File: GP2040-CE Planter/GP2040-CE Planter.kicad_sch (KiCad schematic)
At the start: 57 parts, among them J1 USB_B, J2 USB_A, J3 USB_A, J4 USB_A, J5 USB_A, J6 USB_A, J7 Conn_01x02, U1 TUSB4041IPAPR, U3 TPS2561ADRCR, U4 TPS2561ADRCR, U5 PTMUXHS221NKGR

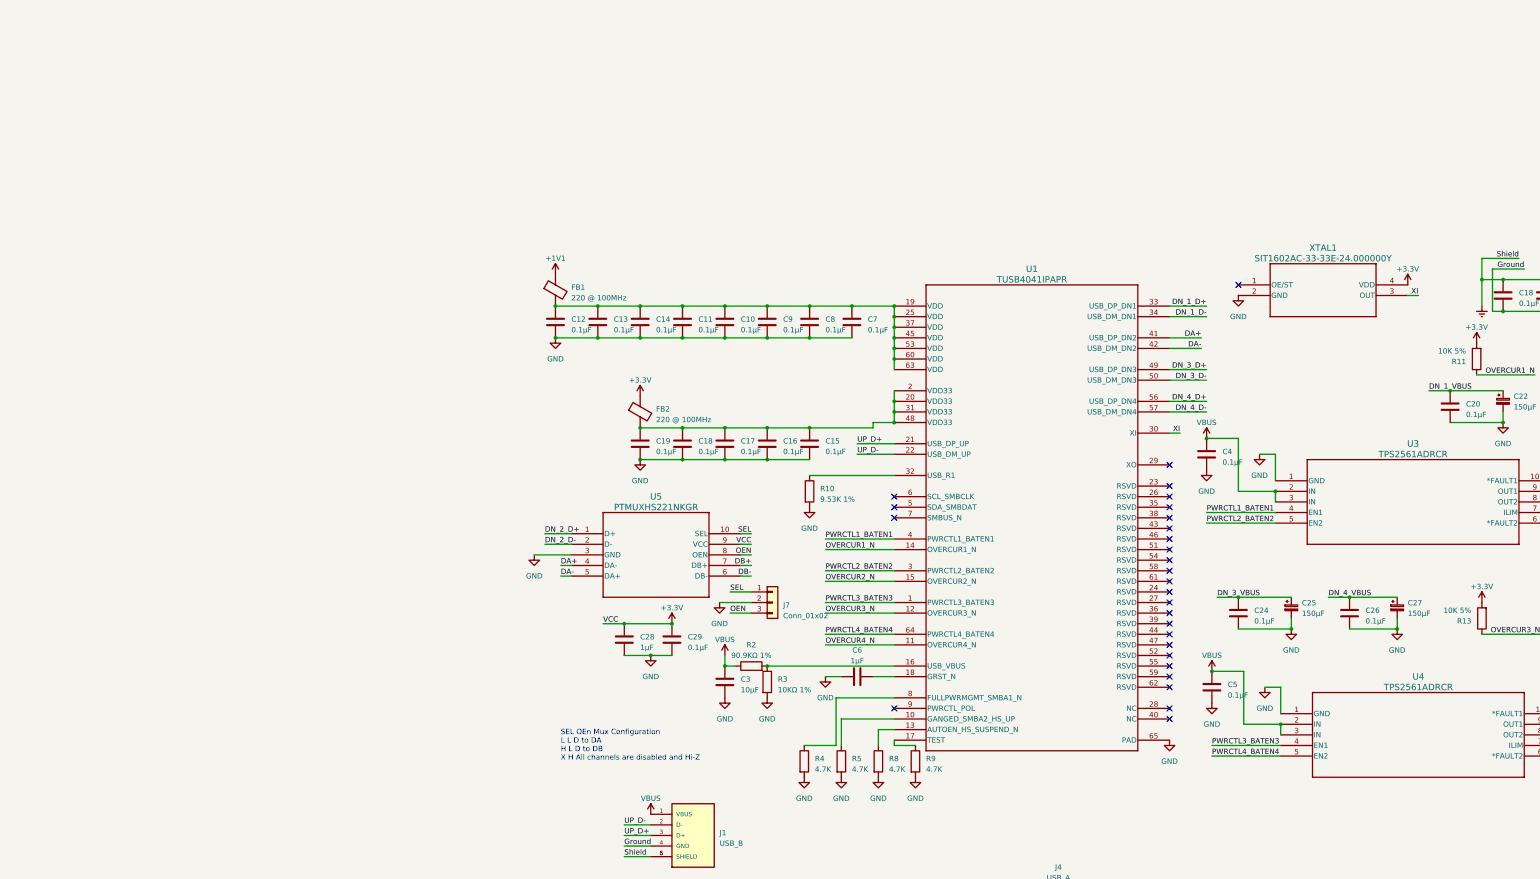
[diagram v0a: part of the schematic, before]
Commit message: Replacing out of stock with instock components
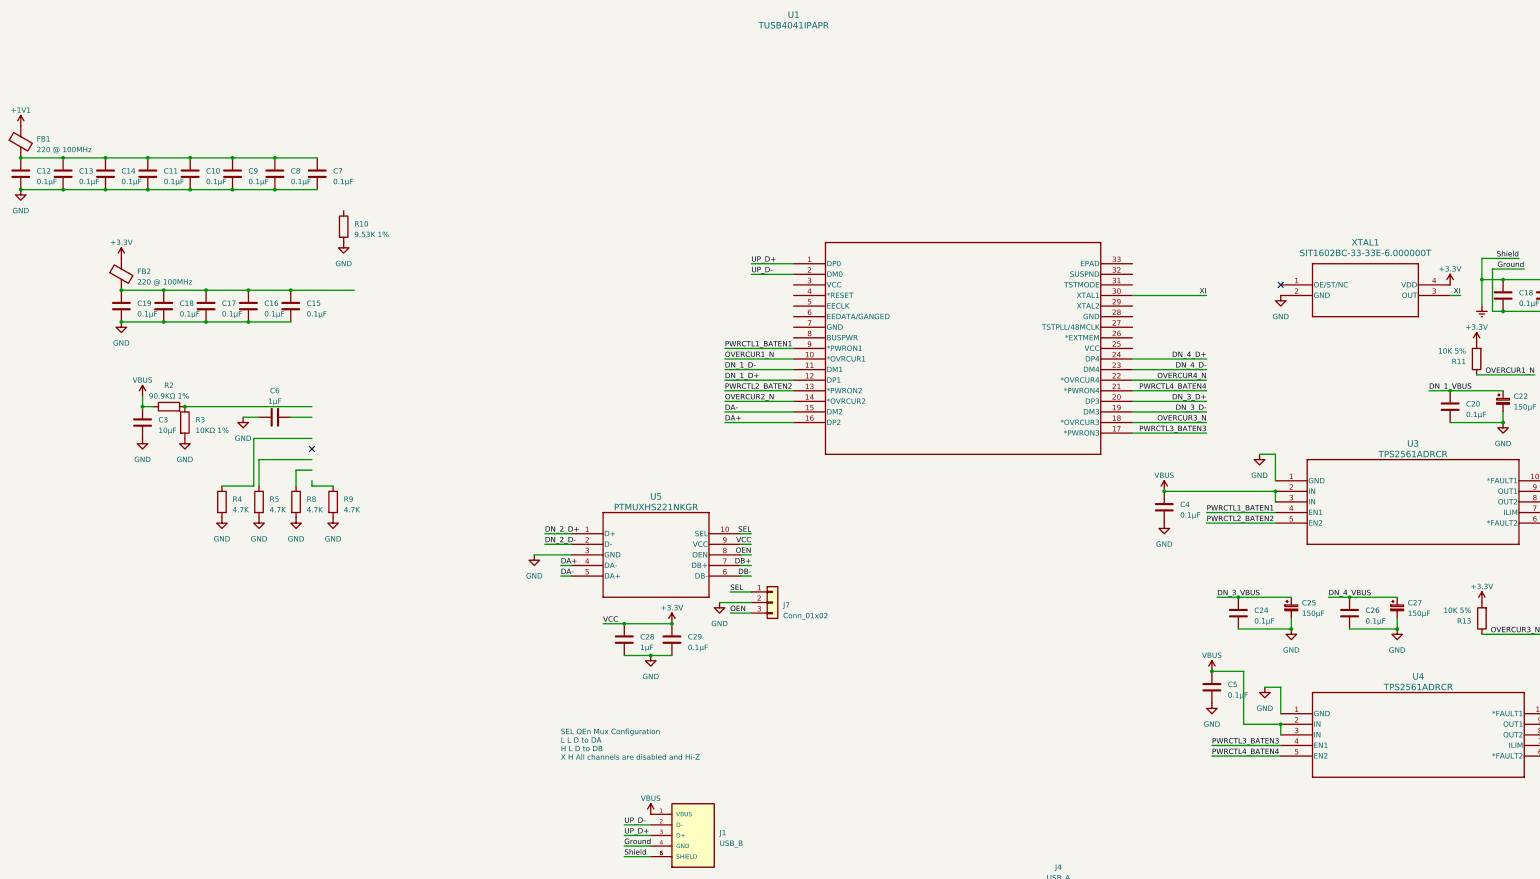
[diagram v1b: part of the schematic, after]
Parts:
- U1: footprint GP2040-CE-Tester:TUSB4041I-Q1 -> GP2040-CE-Tester:RHB32_3P45X3P45_TEX; symbol GP2040-CE-Tester:TUSB4041IPAPR -> GP2040-CE-Tester:TUSB2046IBVF
- XTAL1: value SIT1602AC-33-33E-24.000000Y -> SIT1602BC-33-33E-6.000000T; footprint GP2040-CE-Tester:SIT1602 -> GP2040-CE-Tester:SON4_SIT1602-3_SIT; symbol GP2040-CE-Tester:SIT1602AC-33-33E-24.000000Y -> GP2040-CE-Tester:SIT1602BC-33-33E-6.000000T
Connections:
- net DA+: now also U1.16 (DP2); no longer U1.41 (USB_DP_DN2)
- net DA-: now also U1.15 (DM2); no longer U1.42 (USB_DM_DN2)
- net DN_1_D+: now also U1.12 (DP1); no longer U1.33 (USB_DP_DN1)
- net DN_1_D-: now also U1.11 (DM1); no longer U1.34 (USB_DM_DN1)
- net DN_3_D+: now also U1.20 (DP3); no longer U1.49 (USB_DP_DN3)
- net DN_3_D-: now also U1.19 (DM3); no longer U1.50 (USB_DM_DN3)
- net DN_4_D+: now also U1.24 (DP4); no longer U1.56 (USB_DP_DN4)
- net DN_4_D-: now also U1.23 (DM4); no longer U1.57 (USB_DM_DN4)
- net GND: no longer U1.65 (PAD)
- net OVERCUR1_N: now also U1.10 (*OVRCUR1); no longer U1.14 (OVERCUR1_N)
- net OVERCUR2_N: now also U1.14 (*OVRCUR2); no longer U1.15 (OVERCUR2_N)
- net OVERCUR3_N: now also U1.18 (*OVRCUR3); no longer U1.12 (OVERCUR3_N)
- net OVERCUR4_N: now also U1.22 (*OVRCUR4); no longer U1.11 (OVERCUR4_N)
- net PWRCTL1_BATEN1: now also U1.9 (*PWRON1); no longer U1.4 (PWRCTL1_BATEN1)
- net PWRCTL2_BATEN2: now also U1.13 (*PWRON2); no longer U1.3 (PWRCTL2_BATEN2)
- net PWRCTL3_BATEN3: now also U1.17 (*PWRON3); no longer U1.1 (PWRCTL3_BATEN3)
- net PWRCTL4_BATEN4: now also U1.21 (*PWRON4); no longer U1.64 (PWRCTL4_BATEN4)
- net UP_D+: now also U1.1 (DP0); no longer U1.21 (USB_DP_UP)
- net UP_D-: now also U1.2 (DM0); no longer U1.22 (USB_DM_UP)
- net at C10.1, C11.1, C12.1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: no longer U1.19 (VDD), U1.25 (VDD), U1.37 (VDD), U1.45 (VDD), U1.53 (VDD), U1.60 (VDD), U1.63 (VDD)
- net at C15.1, C16.1, C17.1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: no longer U1.2 (VDD33), U1.20 (VDD33), U1.31 (VDD33), U1.48 (VDD33)
- net at R9.1: no longer U1.17 (TEST)
- net at R5.1: no longer U1.10 (GANGED_SMBA2_HS_UP)
- net at R8.1: no longer U1.13 (AUTOEN_HS_SUSPEND_N)
- net at R2.2, R3.1: no longer U1.16 (USB_VBUS)
- net at C6.2: no longer U1.18 (GRST_N)
- net at U1.32 (SUSPND): no longer R10.1
- net at U1.8 (BUSPWR): no longer R4.1
- no-connect marks 28 -> 2
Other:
- moved on the sheet: C10, C11, C12, C13, C14, C15, C16, C17, C18, C19, C3, C4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

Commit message: ERC passes
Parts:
- removed C10, C11, C12, C13, C14, C15, C16, C17, C18 (x2), C19, C7, C8, C9: 0.1μF, Capacitor_SMD:C_0603_1608Metric, symbol Device:C
- removed C19: 0.001μF, Capacitor_SMD:C_0603_1608Metric, symbol Device:C
- removed C3: 10μF, Capacitor_SMD:C_0603_1608Metric, symbol Device:C
- removed C6: 1μF, Capacitor_SMD:C_0603_1608Metric, symbol Device:C
- removed FB1, FB2: 220 @ 100MHz, Ferrite_THT:LairdTech_28C0236-0JW-10, symbol Device:FerriteBead
- removed R10: 9.53K 1%, Resistor_SMD:R_0603_1608Metric, symbol Device:R
- removed R10: 10KΩ 1%, Resistor_SMD:R_0402_1005Metric, symbol Device:R
- removed R2: 90.9KΩ 1%, Resistor_SMD:R_0603_1608Metric, symbol Device:R
- removed R3: 10KΩ 1%, Resistor_SMD:R_0603_1608Metric, symbol Device:R
- removed R4, R5, R8, R9: 4.7K, Resistor_SMD:R_0603_1608Metric, symbol Device:R
- added C18 (x6), C19 (x6): C, Capacitor_SMD:C_0603_1608Metric, symbol Device:C
- added R10 (x6): R, Resistor_SMD:R_0402_1005Metric, symbol Device:R
- added U3, U4, U5, U6: SN75240PWR, GP2040-CE-Tester:SN75240, symbol GP2040-CE-Tester:SN75240PWR
- C1: renamed from C28; value 1μF -> C
- C15: renamed from C24; value 0.1μF -> C
- C16: renamed from C4; value 0.1μF -> C
- C17: renamed from C5; value 0.1μF -> C
- C18: renamed from C25; value 150μF -> C_Polarized_Small
- C20: renamed from C26; value 0.1μF -> C
- C22: renamed from C27; value 150μF -> C_Polarized_Small
- C23: renamed from C20; value 0.1μF -> C
- C24: renamed from C22; value 150μF -> C_Polarized_Small
- C25: renamed from C21; value 0.1μF -> C
- C26: renamed from C23; value 150μF -> C_Polarized_Small
- C3: renamed from C29; value 0.1μF -> C
- J1: value USB_B -> UJ2-BH-1-TH; footprint GP2040-CE-Tester:GCT_USB1030-XX-X-B-B_REVB -> GP2040-CE-Tester:CUI_UJ2-BH-1-TH; symbol GP2040-CE-Tester:USB1030-XX-X-B-B_REVB -> GP2040-CE-Tester:UJ2-BH-1-TH; MANUFACTURER GCT -> CUI INC; PART_REV (none) -> 1.0; STANDARD (none) -> MANUFACTURER RECOMENDATION
- J2: value USB_A -> UJ2-AH-4-TH; footprint GP2040-CE-Tester:GCT_USB1040-XX-X-X_REVC -> GP2040-CE-Tester:CUI_UJ2-AH-4-TH; symbol GP2040-CE-Tester:USB1040-XX-X-X_REVC -> GP2040-CE-Tester:UJ2-AH-4-TH; MANUFACTURER GCT -> CUI INC; PART_REV (none) -> 1.0; STANDARD (none) -> MANUFACTURER RECOMMENDATIONS
- J3: renamed from J6; value USB_A -> UJ2-AH-4-TH; footprint GP2040-CE-Tester:GCT_USB1040-XX-X-X_REVC -> GP2040-CE-Tester:CUI_UJ2-AH-4-TH; symbol GP2040-CE-Tester:USB1040-XX-X-X_REVC -> GP2040-CE-Tester:UJ2-AH-4-TH; MANUFACTURER GCT -> CUI INC; PART_REV (none) -> 1.0; STANDARD (none) -> MANUFACTURER RECOMMENDATIONS
- J4: renamed from J7; value Conn_01x02 -> Conn_01x03
- J5: renamed from J3; value USB_A -> UJ2-AH-4-TH; footprint GP2040-CE-Tester:GCT_USB1040-XX-X-X_REVC -> GP2040-CE-Tester:CUI_UJ2-AH-4-TH; symbol GP2040-CE-Tester:USB1040-XX-X-X_REVC -> GP2040-CE-Tester:UJ2-AH-4-TH; MANUFACTURER GCT -> CUI INC; PART_REV (none) -> 1.0; STANDARD (none) -> MANUFACTURER RECOMMENDATIONS
- J6: renamed from J4; value USB_A -> UJ2-AH-4-TH; footprint GP2040-CE-Tester:GCT_USB1040-XX-X-X_REVC -> GP2040-CE-Tester:CUI_UJ2-AH-4-TH; symbol GP2040-CE-Tester:USB1040-XX-X-X_REVC -> GP2040-CE-Tester:UJ2-AH-4-TH; MANUFACTURER GCT -> CUI INC; PART_REV (none) -> 1.0; STANDARD (none) -> MANUFACTURER RECOMMENDATIONS
- J7: renamed from J5; value USB_A -> UJ2-AH-4-TH; footprint GP2040-CE-Tester:GCT_USB1040-XX-X-X_REVC -> GP2040-CE-Tester:CUI_UJ2-AH-4-TH; symbol GP2040-CE-Tester:USB1040-XX-X-X_REVC -> GP2040-CE-Tester:UJ2-AH-4-TH; MANUFACTURER GCT -> CUI INC; PART_REV (none) -> 1.0; STANDARD (none) -> MANUFACTURER RECOMMENDATIONS
- R10: renamed from R14; value 10K 5% -> R
- R11: renamed from R12; value 10K 5% -> R
- R12: renamed from R6; value 25.5K 5% -> R
- R13: renamed from R7; value 25.5K 5% -> R
- R8: renamed from R13; value 10K 5% -> R
- R9: renamed from R11; value 10K 5% -> R
- U1: renamed from U5; value PTMUXHS221NKGR -> TMUXHS221NKGR; footprint GP2040-CE-Tester:TMUXHS221N -> GP2040-CE-Tester:UQFN_S221NKGT_TEX; symbol GP2040-CE-Tester:PTMUXHS221NKGR -> GP2040-CE-Tester:TMUXHS221NKGR
- U2: renamed from U1; value TUSB4041IPAPR -> TUSB2046IBVF
- renumbered U4 to U7, U3 to U8
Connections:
- net +3.3V: now also U2.25 (VCC), U2.26 (*EXTMEM), U2.3 (VCC), U2.8 (BUSPWR)
- net DB+: now also U6.2 (C)
- net DB-: now also U6.4 (D)
- net DN_1_D+: now also U4.8 (A)
- net DN_1_D-: now also U4.6 (B)
- net DN_2_D+: now also U4.2 (C)
- net DN_2_D-: now also U4.4 (D)
- net DN_2_VBUS: now also J3.1 (VBUS)
- net DN_3_D+: now also U3.8 (A)
- net DN_3_D-: now also U3.6 (B)
- net DN_4_D+: now also U3.2 (C)
- net DN_4_D-: now also U3.4 (D)
- net Earth: now also J1.SH1 (SHIELD), J1.SH2 (SHIELD__1), J2.SH1 (SHIELD), J2.SH2 (SHIELD__1), J3.SH1 (SHIELD), J3.SH2 (SHIELD__1), J5.SH1 (SHIELD), J5.SH2 (SHIELD__1), J6.SH1 (SHIELD), J6.SH2 (SHIELD__1), J7.SH1 (SHIELD), J7.SH2 (SHIELD__1), C18.2, C18.2, C18.2, C18.2, C18.2, C18.2, C19.2, C19.2, C19.2, C19.2, C19.2, C19.2, R10.2, R10.2, R10.2, R10.2, R10.2, R10.2; no longer J1.5 (SHIELD), J1.6 (SHIELD), J2.5 (SHIELD), J2.6 (SHIELD__1), J3.5 (SHIELD), J3.6 (SHIELD__1), J5.5 (SHIELD), J5.6 (SHIELD__1), J6.5 (SHIELD), J6.6 (SHIELD__1), J7.5 (SHIELD), J7.6 (SHIELD__1)
- net GND: now also C16.1, U2.28 (GND), U2.31 (TSTMODE), U2.33 (EPAD), U2.4 (*RESET), U2.6 (EEDATA/GANGED), U2.7 (GND), C18.1, C18.1, C18.1, C18.1, C18.1, C18.1, C19.1, C19.1, C19.1, C19.1, C19.1, C19.1, R10.1, R10.1, R10.1, R10.1, R10.1, R10.1, U3.1 (GND), U3.3 (GND), U3.5 (GND), U3.7 (GND), U4.1 (GND), U4.3 (GND), U4.5 (GND), U4.7 (GND), U5.1 (GND), U5.3 (GND), U5.5 (GND), U5.7 (GND), U6.1 (GND), U6.3 (GND), U6.5 (GND), U6.7 (GND); no longer C16.2
- net UP_D+: now also U5.2 (C)
- net UP_D-: now also U5.4 (D)
- net VBUS: now also C16.2; no longer C16.1
- no-connect marks 2 -> 9
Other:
- moved on the sheet: C1, C15, C16, C17, C18, C20, C22, C23, C24, C25, C26, C3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

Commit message: Dueling Picos!
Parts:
- removed C15, C17, C18 (x2), C19 (x2), C20: C, Capacitor_SMD:C_0603_1608Metric, symbol Device:C
- removed C18, C22: C_Polarized_Small, Capacitor_SMD:CP_Elec_3x5.3, symbol Device:C_Polarized_Small
- removed J6, J7: UJ2-AH-4-TH, GP2040-CE-Tester:CUI_UJ2-AH-4-TH, symbol GP2040-CE-Tester:UJ2-AH-4-TH
- removed R10, R13, R8: R, Resistor_SMD:R_0603_1608Metric, symbol Device:R
- removed R10 (x2): R, Resistor_SMD:R_0402_1005Metric, symbol Device:R
- removed U3: SN75240PWR, GP2040-CE-Tester:SN75240, symbol GP2040-CE-Tester:SN75240PWR
- removed U7: TPS2561ADRCR, GP2040-CE-Tester:DRC10_2P4X1P65_TEX, symbol GP2040-CE-Tester:TPS2561ADRCR
- added C12, C16: C, Capacitor_SMD:C_0603_1608Metric, symbol Device:C
- added H1, H2, H3, H4: MountingHole, MountingHole:MountingHole_2.5mm, symbol Mechanical:MountingHole
- added U7: TLV73333PDBVR, GP2040-CE-Tester:TLV7333P, symbol GP2040-CE-Tester:TLV73333PDBVR
- C14: renamed from C24; footprint Capacitor_SMD:CP_Elec_3x5.3 -> GP2040-CE-Tester:CAP_RHA&slash_HS_8X6P7_NCH
- C17: renamed from C26; footprint Capacitor_SMD:CP_Elec_3x5.3 -> GP2040-CE-Tester:CAP_RHA&slash_HS_8X6P7_NCH
- J3: value UJ2-AH-4-TH -> UJ2-BH-1-TH; footprint GP2040-CE-Tester:CUI_UJ2-AH-4-TH -> GP2040-CE-Tester:CUI_UJ2-BH-1-TH; symbol GP2040-CE-Tester:UJ2-AH-4-TH -> GP2040-CE-Tester:UJ2-BH-1-TH; STANDARD MANUFACTURER RECOMMENDATIONS -> MANUFACTURER RECOMENDATION
- U1: footprint GP2040-CE-Tester:UQFN_S221NKGT_TEX -> GP2040-CE-Tester:TMUXHS221
- renumbered C16 to C11, C23 to C13, C25 to C15, C1 to C3, C3 to C4, R9 to R5, R11 to R6, R12 to R7, U4 to U3, U5 to U4, U6 to U5, U8 to U6
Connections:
- net +3.3V: now also C12.1, U7.5 (OUT)
- net DN_1_VBUS: now also U6.8 (OUT2); no longer U6.9 (OUT1)
- net DN_2_VBUS: now also U6.9 (OUT1); no longer U6.8 (OUT2)
- net GND: now also C12.2, C16.2, U7.2 (GND)
- net VBUS: now also C16.1, U7.1 (IN), U7.3 (EN)
- net DN_3_D+: no longer names the net of U2.20 (DP3)
- net DN_3_D-: no longer names the net of U2.19 (DM3)
- net DN_4_D+: no longer names the net of U2.24 (DP4)
- net DN_4_D-: no longer names the net of U2.23 (DM4)
- net OVERCUR3_N: no longer names the net of U2.18 (*OVRCUR3)
- net OVERCUR4_N: no longer names the net of U2.22 (*OVRCUR4)
- net PWRCTL3_BATEN3: no longer names the net of U2.17 (*PWRON3)
- net PWRCTL4_BATEN4: no longer names the net of U2.21 (*PWRON4)
- no-connect marks 9 -> 18
